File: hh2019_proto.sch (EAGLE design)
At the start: 146 parts, among them IC1 CP210X_USB_UART, IC2 AP2114H, IC4 TP4056, J1 PJ-313D, Q1 MMBT2222A, Q3 MMBT2222A, Q4 MMBT2222A, Q5 SI1304 BDL, T1 MOSFET-PCHANNEL, T2 MOSFET-PCHANNEL, U1 MPR121QR2, U2 ESP32-WROVER-I, U3 PCM5102A, X4 JST-PH3

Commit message: Added net names for touch controller pins (will remap touch buttons for easy routing later)
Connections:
- net N$1 renamed ELE1
- net N$24 renamed ELE2
- net N$25 renamed ELE3
- net N$44 renamed ELE4
- net N$46 renamed ELE7
- net N$47 renamed ELE6
- net N$48 renamed ELE5
- net N$6 renamed ELE0
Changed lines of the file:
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@@
 </segment>
 </net>
-<net name="N$44" class="3">
+<net name="ELE4" class="3">
 <segment>
 <pinref part="TOUCH_SEL" gate="G$1" pin="DOWN"/>
@@
 </segment>
 </net>
-<net name="N$6" class="3">
+<net name="ELE0" class="3">
 <segment>
 <pinref part="TOUCH_A" gate="G$1" pin="P$1"/>
@@
 </segment>
 </net>
-<net name="N$1" class="3">
+<net name="ELE1" class="3">
 <segment>
 <pinref part="U1" gate="A" pin="ELE1"/>
@@
 </segment>
 </net>
-<net name="N$24" class="3">
+<net name="ELE2" class="3">
 <segment>
 <pinref part="U1" gate="A" pin="ELE2"/>
@@
 </segment>
 </net>
-<net name="N$25" class="3">
+<net name="ELE3" class="3">
 <segment>
 <pinref part="U1" gate="A" pin="ELE3"/>
@@
 </segment>
 </net>
-<net name="N$46" class="3">
+<net name="ELE7" class="3">
 <segment>
 <pinref part="U1" gate="A" pin="ELE7"/>
@@
 </segment>
 </net>
-<net name="N$47" class="3">
+<net name="ELE6" class="3">
 <segment>
 <pinref part="U1" gate="A" pin="ELE6"/>
@@
 </segment>
 </net>
-<net name="N$48" class="3">
+<net name="ELE5" class="3">
 <segment>
 <pinref part="U1" gate="A" pin="ELE5"/>

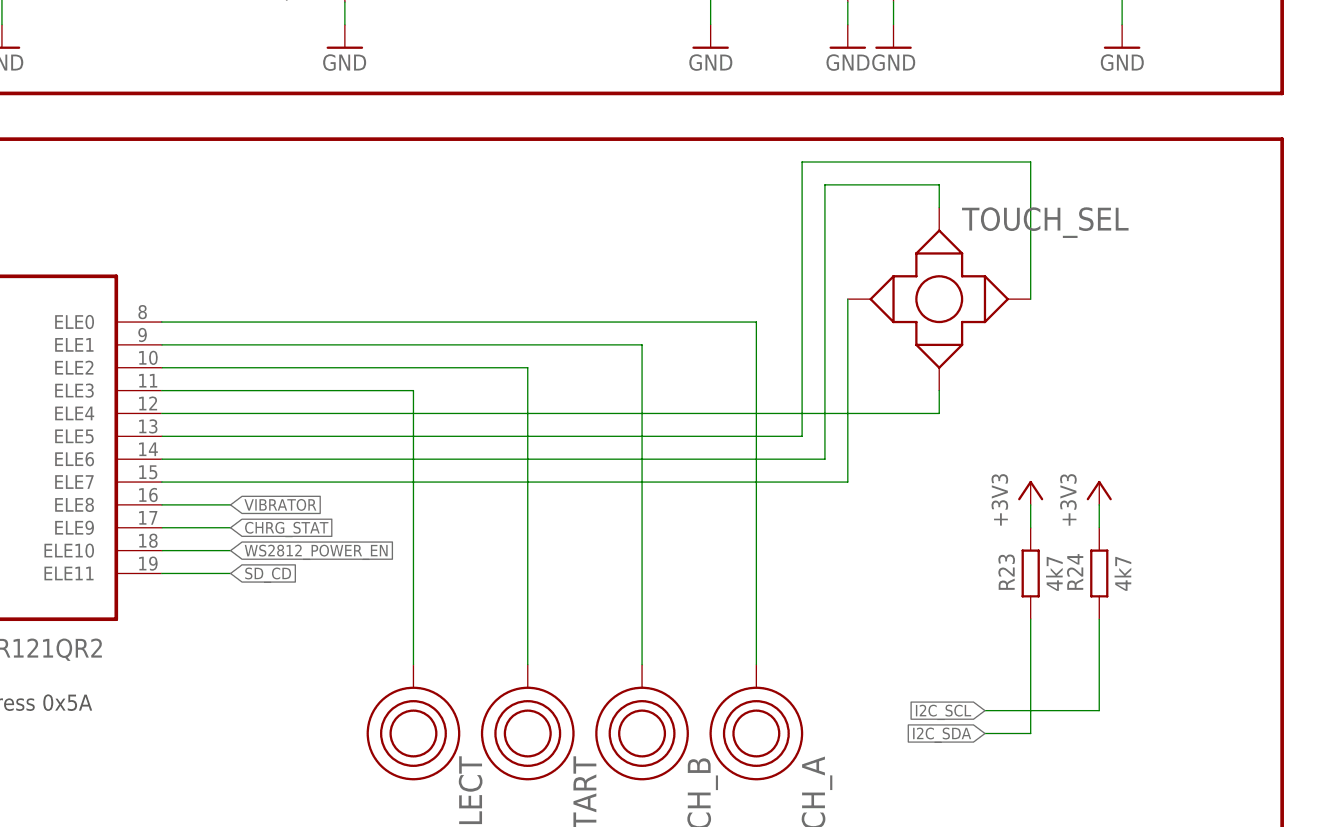
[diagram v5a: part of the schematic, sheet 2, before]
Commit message: Reassigned touch controller pins for easier layouting, got proper main component placement on board
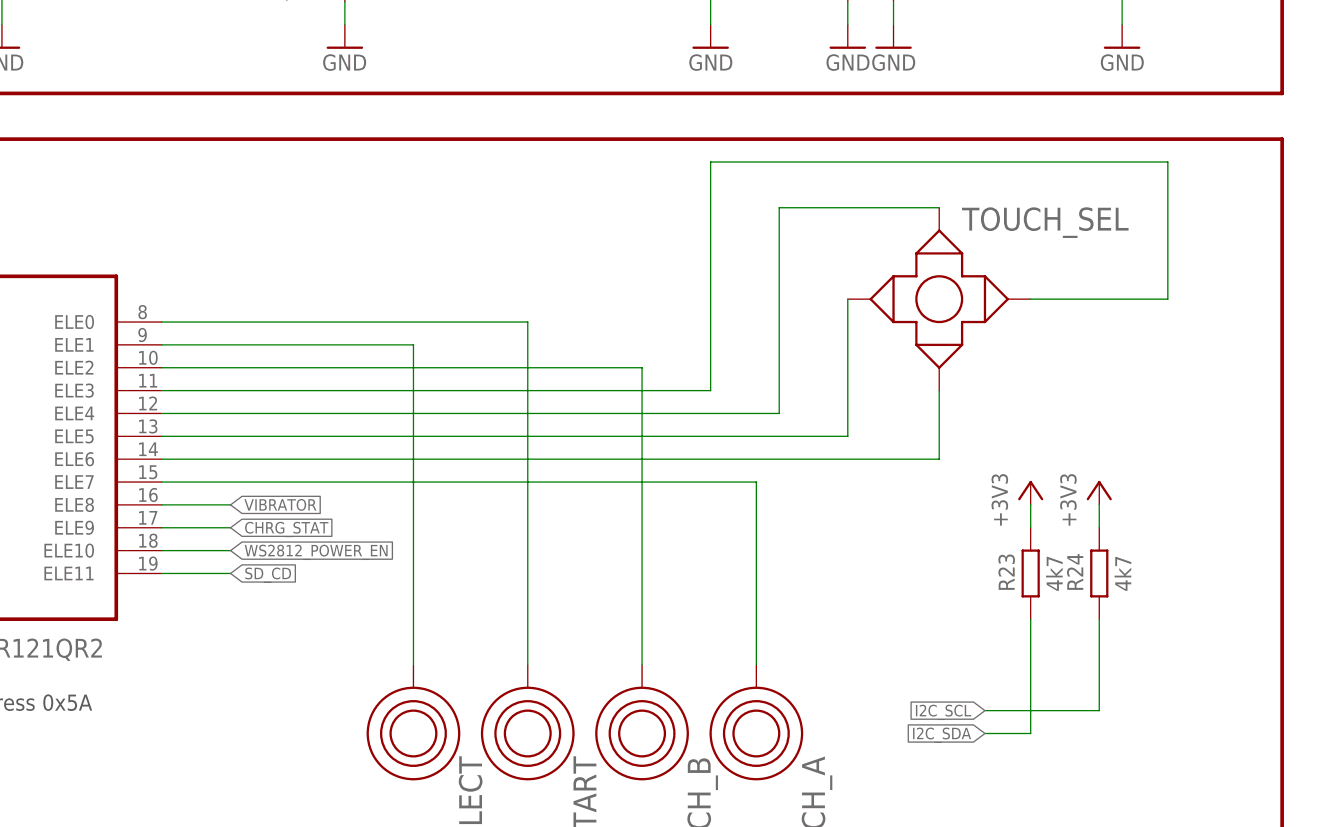
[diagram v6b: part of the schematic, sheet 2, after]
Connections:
- net ELE0: now also TOUCH_START.P$1; no longer TOUCH_A.P$1
- net ELE1: now also TOUCH_SELECT.P$1; no longer TOUCH_B.P$1
- net ELE2: now also TOUCH_B.P$1; no longer TOUCH_START.P$1
- net ELE3: now also TOUCH_SEL.RIGHT; no longer TOUCH_SELECT.P$1
- net ELE4: now also TOUCH_SEL.UP; no longer TOUCH_SEL.DOWN
- net ELE5: now also TOUCH_SEL.LEFT; no longer TOUCH_SEL.RIGHT
- net ELE6: now also TOUCH_SEL.DOWN; no longer TOUCH_SEL.UP
- net ELE7: now also TOUCH_A.P$1; no longer TOUCH_SEL.LEFT
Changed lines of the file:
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@@
 <net name="ELE4" class="3">
 <segment>
-<pinref part="TOUCH_SEL" gate="G$1" pin="DOWN"/>
 <pinref part="U1" gate="A" pin="ELE4"/>
-<wire x1="104.14" y1="83.82" x2="190.5" y2="83.82" width="0.1524" layer="91"/>
-<wire x1="190.5" y1="83.82" x2="190.5" y2="86.36" width="0.1524" layer="91"/>
+<wire x1="104.14" y1="83.82" x2="172.72" y2="83.82" width="0.1524" layer="91"/>
+<pinref part="TOUCH_SEL" gate="G$1" pin="UP"/>
+<wire x1="172.72" y1="83.82" x2="172.72" y2="106.68" width="0.1524" layer="91"/>
+<wire x1="172.72" y1="106.68" x2="190.5" y2="106.68" width="0.1524" layer="91"/>
 </segment>
 </net>
 <net name="ELE0" class="3">
 <segment>
-<pinref part="TOUCH_A" gate="G$1" pin="P$1"/>
-<wire x1="170.18" y1="93.98" x2="170.18" y2="55.88" width="0.1524" layer="91"/>
 <pinref part="U1" gate="A" pin="ELE0"/>
-<wire x1="104.14" y1="93.98" x2="170.18" y2="93.98" width="0.1524" layer="91"/>
+<wire x1="104.14" y1="93.98" x2="144.78" y2="93.98" width="0.1524" layer="91"/>
+<wire x1="144.78" y1="93.98" x2="144.78" y2="55.88" width="0.1524" layer="91"/>
+<pinref part="TOUCH_START" gate="G$1" pin="P$1"/>
 </segment>
 </net>
@@
 <segment>
 <pinref part="U1" gate="A" pin="ELE1"/>
-<pinref part="TOUCH_B" gate="G$1" pin="P$1"/>
-<wire x1="104.14" y1="91.44" x2="157.48" y2="91.44" width="0.1524" layer="91"/>
-<wire x1="157.48" y1="91.44" x2="157.48" y2="55.88" width="0.1524" layer="91"/>
+<wire x1="104.14" y1="91.44" x2="132.08" y2="91.44" width="0.1524" layer="91"/>
+<pinref part="TOUCH_SELECT" gate="G$1" pin="P$1"/>
+<wire x1="132.08" y1="91.44" x2="132.08" y2="55.88" width="0.1524" layer="91"/>
 </segment>
 </net>
@@
 <segment>
 <pinref part="U1" gate="A" pin="ELE2"/>
-<pinref part="TOUCH_START" gate="G$1" pin="P$1"/>
-<wire x1="104.14" y1="88.9" x2="144.78" y2="88.9" width="0.1524" layer="91"/>
-<wire x1="144.78" y1="88.9" x2="144.78" y2="55.88" width="0.1524" layer="91"/>
+<wire x1="104.14" y1="88.9" x2="157.48" y2="88.9" width="0.1524" layer="91"/>
+<pinref part="TOUCH_B" gate="G$1" pin="P$1"/>
+<wire x1="157.48" y1="88.9" x2="157.48" y2="55.88" width="0.1524" layer="91"/>
 </segment>
 </net>
@@
 <segment>
 <pinref part="U1" gate="A" pin="ELE3"/>
-<pinref part="TOUCH_SELECT" gate="G$1" pin="P$1"/>
-<wire x1="104.14" y1="86.36" x2="132.08" y2="86.36" width="0.1524" layer="91"/>
-<wire x1="132.08" y1="86.36" x2="132.08" y2="55.88" width="0.1524" layer="91"/>
+<wire x1="104.14" y1="86.36" x2="165.1" y2="86.36" width="0.1524" layer="91"/>
+<wire x1="165.1" y1="86.36" x2="165.1" y2="111.76" width="0.1524" layer="91"/>
+<wire x1="165.1" y1="111.76" x2="215.9" y2="111.76" width="0.1524" layer="91"/>
+<wire x1="215.9" y1="111.76" x2="215.9" y2="96.52" width="0.1524" layer="91"/>
+<pinref part="TOUCH_SEL" gate="G$1" pin="RIGHT"/>
+<wire x1="215.9" y1="96.52" x2="200.66" y2="96.52" width="0.1524" layer="91"/>
 </segment>
 </net>
@@
 <segment>
 <pinref part="U1" gate="A" pin="ELE7"/>
-<pinref part="TOUCH_SEL" gate="G$1" pin="LEFT"/>
-<wire x1="104.14" y1="76.2" x2="180.34" y2="76.2" width="0.1524" layer="91"/>
-<wire x1="180.34" y1="76.2" x2="180.34" y2="96.52" width="0.1524" layer="91"/>
+<wire x1="104.14" y1="76.2" x2="170.18" y2="76.2" width="0.1524" layer="91"/>
+<pinref part="TOUCH_A" gate="G$1" pin="P$1"/>
+<wire x1="170.18" y1="76.2" x2="170.18" y2="55.88" width="0.1524" layer="91"/>
 </segment>
 </net>
@@
 <segment>
 <pinref part="U1" gate="A" pin="ELE6"/>
-<wire x1="104.14" y1="78.74" x2="177.8" y2="78.74" width="0.1524" layer="91"/>
-<wire x1="177.8" y1="78.74" x2="177.8" y2="109.22" width="0.1524" layer="91"/>
-<pinref part="TOUCH_SEL" gate="G$1" pin="UP"/>
-<wire x1="177.8" y1="109.22" x2="190.5" y2="109.22" width="0.1524" layer="91"/>
-<wire x1="190.5" y1="109.22" x2="190.5" y2="106.68" width="0.1524" layer="91"/>
+<wire x1="104.14" y1="78.74" x2="190.5" y2="78.74" width="0.1524" layer="91"/>
+<pinref part="TOUCH_SEL" gate="G$1" pin="DOWN"/>
+<wire x1="190.5" y1="78.74" x2="190.5" y2="86.36" width="0.1524" layer="91"/>
 </segment>
 </net>
@@
 <segment>
 <pinref part="U1" gate="A" pin="ELE5"/>
-<wire x1="104.14" y1="81.28" x2="175.26" y2="81.28" width="0.1524" layer="91"/>
-<wire x1="175.26" y1="81.28" x2="175.26" y2="111.76" width="0.1524" layer="91"/>
-<pinref part="TOUCH_SEL" gate="G$1" pin="RIGHT"/>
-<wire x1="175.26" y1="111.76" x2="200.66" y2="111.76" width="0.1524" layer="91"/>
-<wire x1="200.66" y1="111.76" x2="200.66" y2="96.52" width="0.1524" layer="91"/>
+<wire x1="104.14" y1="81.28" x2="180.34" y2="81.28" width="0.1524" layer="91"/>
+<pinref part="TOUCH_SEL" gate="G$1" pin="LEFT"/>
+<wire x1="180.34" y1="81.28" x2="180.34" y2="96.52" width="0.1524" layer="91"/>
 </segment>
 </net>

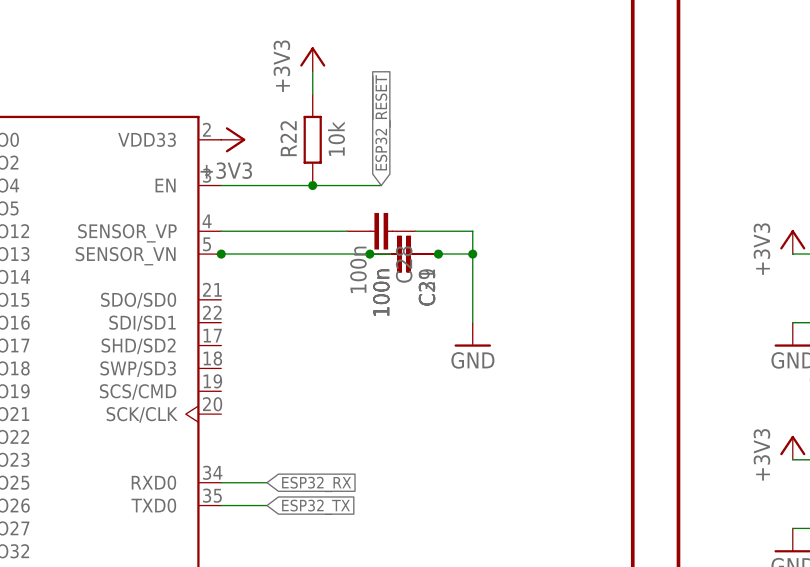
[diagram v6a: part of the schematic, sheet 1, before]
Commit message: Placed major components, working on passives
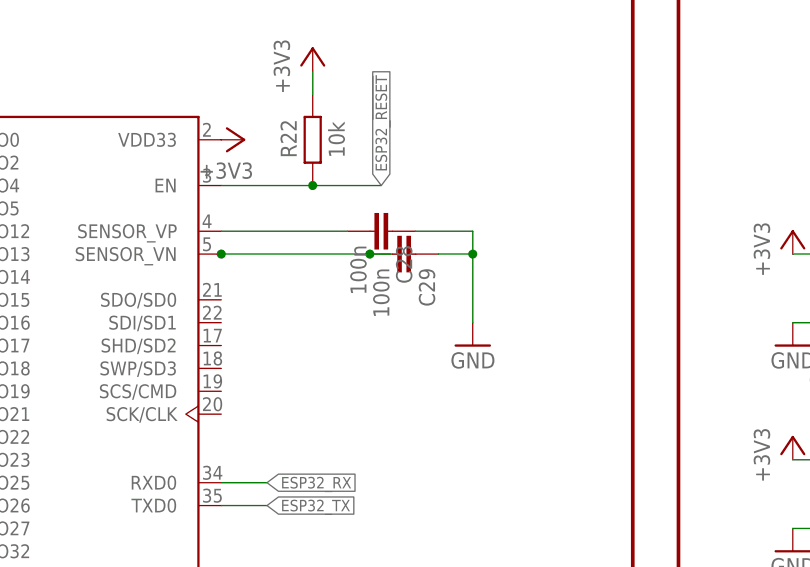
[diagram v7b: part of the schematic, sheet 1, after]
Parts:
- removed C31: 100n, hh2019_proto:C0603-DASHES
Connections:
- net GND: no longer C31.1
- net N$43: no longer C31.2
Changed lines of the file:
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@@
 <part name="U3" library="DMF-TI_DIR9001" deviceset="PCM5102A" device=""/>
 <part name="J1" library="audioconn" deviceset="PJ-313" device="D"/>
-<part name="C31" library="hh2019_proto" deviceset="C0603-DASHES" device="" value="100n">
-<attribute name="MF" value=""/>
-<attribute name="MPN" value=""/>
-<attribute name="OC_FARNELL" value="unknown"/>
-<attribute name="PARTNO" value="GRM188R71H104KA93D"/>
-</part>
 <part name="C37" library="rcl" library_urn="urn:adsk.eagle:library:334" deviceset="C-EU" device="C0603" package3d_urn="urn:adsk.eagle:package:23616/2" value="100n"/>
 <part name="C40" library="rcl" library_urn="urn:adsk.eagle:library:334" deviceset="C-EU" device="C0603" package3d_urn="urn:adsk.eagle:package:23616/2" value="1u"/>
@@
 <attribute name="VALUE" x="139.7" y="50.8" size="1.778" layer="96"/>
 </instance>
-<instance part="C31" gate="G$1" x="101.6" y="114.3" smashed="yes" rot="R270">
-<attribute name="OC_FARNELL" x="101.6" y="114.3" size="1.778" layer="96" rot="MR90" display="off"/>
-<attribute name="MF" x="101.6" y="114.3" size="1.778" layer="96" rot="MR90" display="off"/>
-<attribute name="MPN" x="101.6" y="114.3" size="1.778" layer="96" rot="MR90" display="off"/>
-<attribute name="PARTNO" x="101.6" y="114.3" size="1.778" layer="96" rot="R180" display="off"/>
-<attribute name="NAME" x="103.251" y="112.776" size="1.778" layer="95" rot="R270"/>
-<attribute name="VALUE" x="98.171" y="112.776" size="1.778" layer="96" rot="R270"/>
-</instance>
 <instance part="C37" gate="G$1" x="200.66" y="121.92" smashed="yes" rot="R180">
 <attribute name="NAME" x="199.136" y="121.539" size="1.778" layer="95" rot="R180"/>
@@
 <pinref part="C29" gate="G$1" pin="1"/>
 <pinref part="GND5" gate="1" pin="GND"/>
-<pinref part="C31" gate="G$1" pin="1"/>
-<junction x="105.41" y="114.3"/>
 <wire x1="109.22" y1="114.3" x2="109.22" y2="106.68" width="0.1524" layer="91"/>
 <wire x1="105.41" y1="114.3" x2="109.22" y2="114.3" width="0.1524" layer="91"/>
@@
 <wire x1="97.79" y1="114.3" x2="100.076" y2="114.3" width="0.1524" layer="91"/>
 <junction x="97.79" y="114.3"/>
-<pinref part="C31" gate="G$1" pin="2"/>
-</segment>
-</net>
+</segment>
+</net>

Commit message: Added most non-bypass passives
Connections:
- new net BAT: C34.1, F2.1, IC4.BAT, X43.1
- net VBAT: no longer C34.1, F2.1, IC4.BAT, X43.1
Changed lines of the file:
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@@
 <pinref part="U$8" gate="G$1" pin="VBAT"/>
-</segment>
-<segment>
-<wire x1="124.46" y1="137.16" x2="92.71" y2="137.16" width="0.1524" layer="91"/>
-<wire x1="71.12" y1="137.16" x2="92.71" y2="137.16" width="0.1524" layer="91"/>
-<wire x1="92.71" y1="137.16" x2="92.71" y2="139.7" width="0.1524" layer="91"/>
-<junction x="92.71" y="137.16"/>
-<pinref part="X4" gate="3" pin="1"/>
-<pinref part="F2" gate="G$1" pin="1"/>
-<pinref part="C34" gate="G$1" pin="1"/>
-<pinref part="IC4" gate="G$1" pin="BAT"/>
-<wire x1="124.46" y1="137.16" x2="132.08" y2="137.16" width="0.1524" layer="91"/>
-<junction x="124.46" y="137.16"/>
 </segment>
 </net>
@@
 </segment>
 </net>
+<net name="BAT" class="1">
+<segment>
+<wire x1="124.46" y1="137.16" x2="92.71" y2="137.16" width="0.1524" layer="91"/>
+<pinref part="X4" gate="3" pin="1"/>
+<pinref part="C34" gate="G$1" pin="1"/>
+<pinref part="IC4" gate="G$1" pin="BAT"/>
+<wire x1="91.44" y1="137.16" x2="71.12" y2="137.16" width="0.1524" layer="91"/>
+<wire x1="124.46" y1="137.16" x2="132.08" y2="137.16" width="0.1524" layer="91"/>
+<junction x="124.46" y="137.16"/>
+<pinref part="F2" gate="G$1" pin="1"/>
+<wire x1="92.71" y1="139.7" x2="92.71" y2="137.16" width="0.1524" layer="91"/>
+<wire x1="92.71" y1="137.16" x2="91.44" y2="137.16" width="0.1524" layer="91"/>
+</segment>
+</net>
